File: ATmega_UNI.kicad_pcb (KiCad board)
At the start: 2 copper layers, 53.3 x 68.6 mm, 61 parts, among them J1 PDIP_1_to_14, J11 PDIP_1_to_14, J2 PDIP_15_to_28, J22 PDIP_15_to_28, J611 I2C, J612 I2C, J613 I2C, J62 4uni, J63 4uni, J64 4uni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

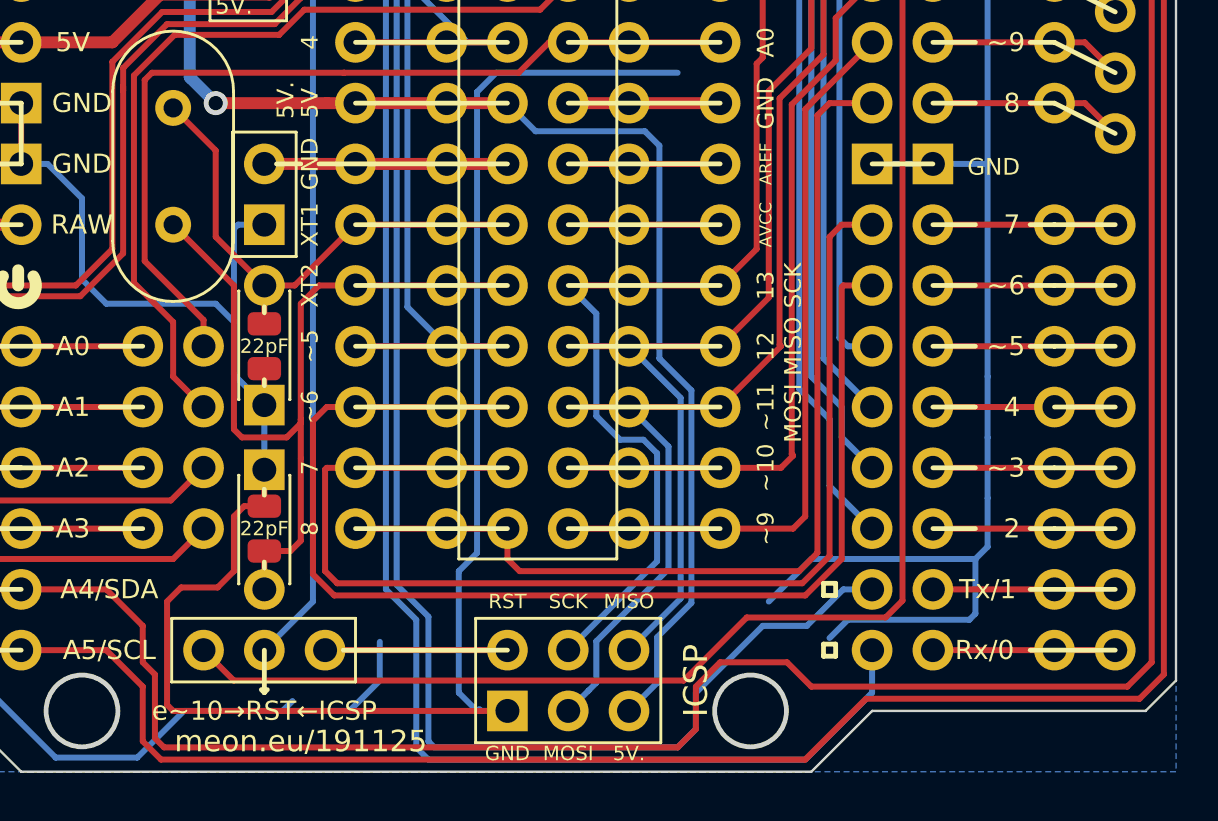
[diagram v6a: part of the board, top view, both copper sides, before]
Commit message: add one more extra gnd pin
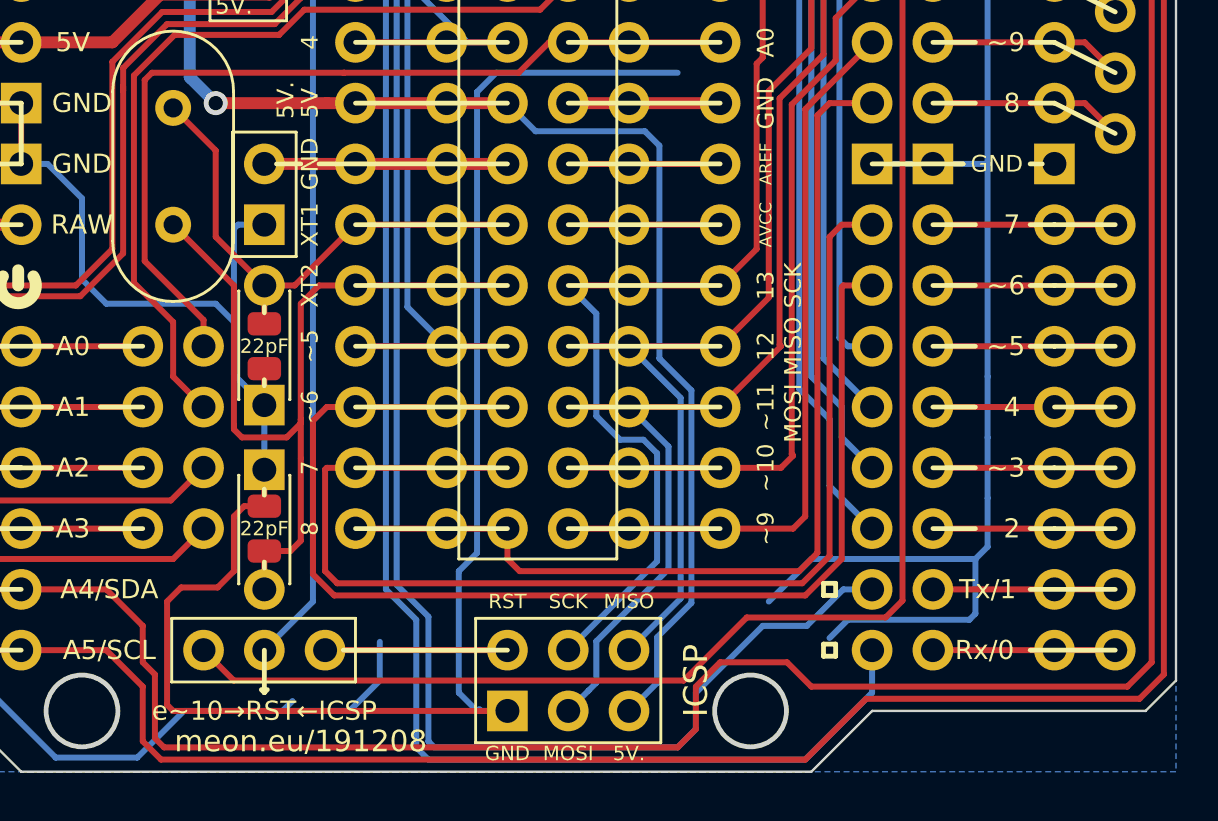
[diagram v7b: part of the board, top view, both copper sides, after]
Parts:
- added J100: extra_gnd, Connector_PinHeader_2.54mm:PinHeader_1x01_P2.54mm_Vertical_no_lines, F.Cu at (114.3, 88.9)
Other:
- board text added: "meon.eu/191208"
- board text removed: "meon.eu/191125"
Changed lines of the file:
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@@
   (general
     (thickness 1.6)
-    (drawings 580)
+    (drawings 582)
     (tracks 748)
     (zones 0)
-    (modules 61)
+    (modules 62)
     (nets 72)
   )
@@
     )
   )
+  (module Connector_PinHeader_2.54mm:PinHeader_1x01_P2.54mm_Vertical_no_lines (layer F.Cu)
+    (at 114.3 88.9)
+    (descr "Through hole straight pin header, 1x01, 2.54mm pitch, single row")
+    (tags "Through hole pin header THT 1x01 2.54mm single row")
+    (fp_text reference J100 (at 0 -2.33) (layer F.SilkS) hide
+      (effects (font (size 1 1) (thickness 0.15)))
+    )
+    (fp_text value extra_gnd (at 0 2.33) (layer F.Fab) hide
+      (effects (font (size 1 1) (thickness 0.15)))
+    )
+    (fp_line (start -0.635 -1.27) (end 1.27 -1.27) (layer F.Fab) (width 0.1))
+    (fp_line (start 1.27 -1.27) (end 1.27 1.27) (layer F.Fab) (width 0.1))
+    (fp_line (start 1.27 1.27) (end -1.27 1.27) (layer F.Fab) (width 0.1))
+    (fp_line (start -1.27 1.27) (end -1.27 -0.635) (layer F.Fab) (width 0.1))
+    (fp_line (start -1.27 -0.635) (end -0.635 -1.27) (layer F.Fab) (width 0.1))
+    (fp_line (start -1.8 -1.8) (end -1.8 1.8) (layer F.CrtYd) (width 0.05))
+    (fp_line (start -1.8 1.8) (end 1.8 1.8) (layer F.CrtYd) (width 0.05))
+    (fp_line (start 1.8 1.8) (end 1.8 -1.8) (layer F.CrtYd) (width 0.05))
+    (fp_line (start 1.8 -1.8) (end -1.8 -1.8) (layer F.CrtYd) (width 0.05))
+    (fp_text user %R (at 0 0 90) (layer F.Fab) hide
+      (effects (font (size 1 1) (thickness 0.15)))
+    )
+    (pad 1 thru_hole rect (at 0 0) (size 1.7 1.7) (drill 1) (layers *.Cu *.Mask)
+      (net 23 GND))
+    (model ${KISYS3DMOD}/Connector_PinHeader_2.54mm.3dshapes/PinHeader_1x01_P2.54mm_Vertical.wrl
+      (at (xyz 0 0 0))
+      (scale (xyz 1 1 1))
+      (rotate (xyz 0 0 0))
+    )
+  )
+  (gr_line (start 113.284 88.9) (end 113.792 88.9) (layer B.SilkS) (width 0.2))
+  (gr_line (start 113.284 88.9) (end 113.792 88.9) (layer F.SilkS) (width 0.2))
   (gr_line (start 75.692 70.612) (end 76.708 70.612) (layer B.SilkS) (width 0.2))
   (gr_line (start 75.692 70.612) (end 76.708 70.612) (layer F.SilkS) (width 0.2))
@@
   (gr_line (start 82.042 62.23) (end 85.217 62.23) (layer F.SilkS) (width 0.2))
   (gr_line (start 82.042 64.77) (end 85.217 64.77) (layer F.SilkS) (width 0.2))
-  (gr_text GND (at 111.76 89.027) (layer B.SilkS)
+  (gr_text GND (at 111.887 88.9) (layer B.SilkS)
     (effects (font (size 0.7 0.7) (thickness 0.15)) (justify mirror))
   )
-  (gr_text GND (at 111.76 89.027) (layer F.SilkS)
+  (gr_text GND (at 111.887 88.9) (layer F.SilkS)
     (effects (font (size 0.7 0.7) (thickness 0.15)))
   )
@@
     (effects (font (size 0.7 0.7) (thickness 0.15)))
   )
-  (gr_line (start 106.68 88.9) (end 109.22 88.9) (layer B.SilkS) (width 0.2))
-  (gr_line (start 106.68 88.9) (end 109.22 88.9) (layer F.SilkS) (width 0.2))
-  (gr_text meon.eu/191125 (at 82.804 113.03) (layer F.SilkS)
+  (gr_line (start 106.68 88.9) (end 110.49 88.9) (layer B.SilkS) (width 0.2))
+  (gr_line (start 106.68 88.9) (end 110.49 88.9) (layer F.SilkS) (width 0.2))
+  (gr_text meon.eu/191208 (at 82.804 113.03) (layer F.SilkS)
     (effects (font (size 0.9 0.9) (thickness 0.2)))
   )
@@
     (effects (font (size 0.7 0.7) (thickness 0.15)))
   )
-  (gr_text meon.eu/191125 (at 82.804 113.03) (layer B.SilkS)
+  (gr_text meon.eu/191208 (at 82.804 113.03) (layer B.SilkS)
     (effects (font (size 0.9 0.9) (thickness 0.2)) (justify mirror))
   )

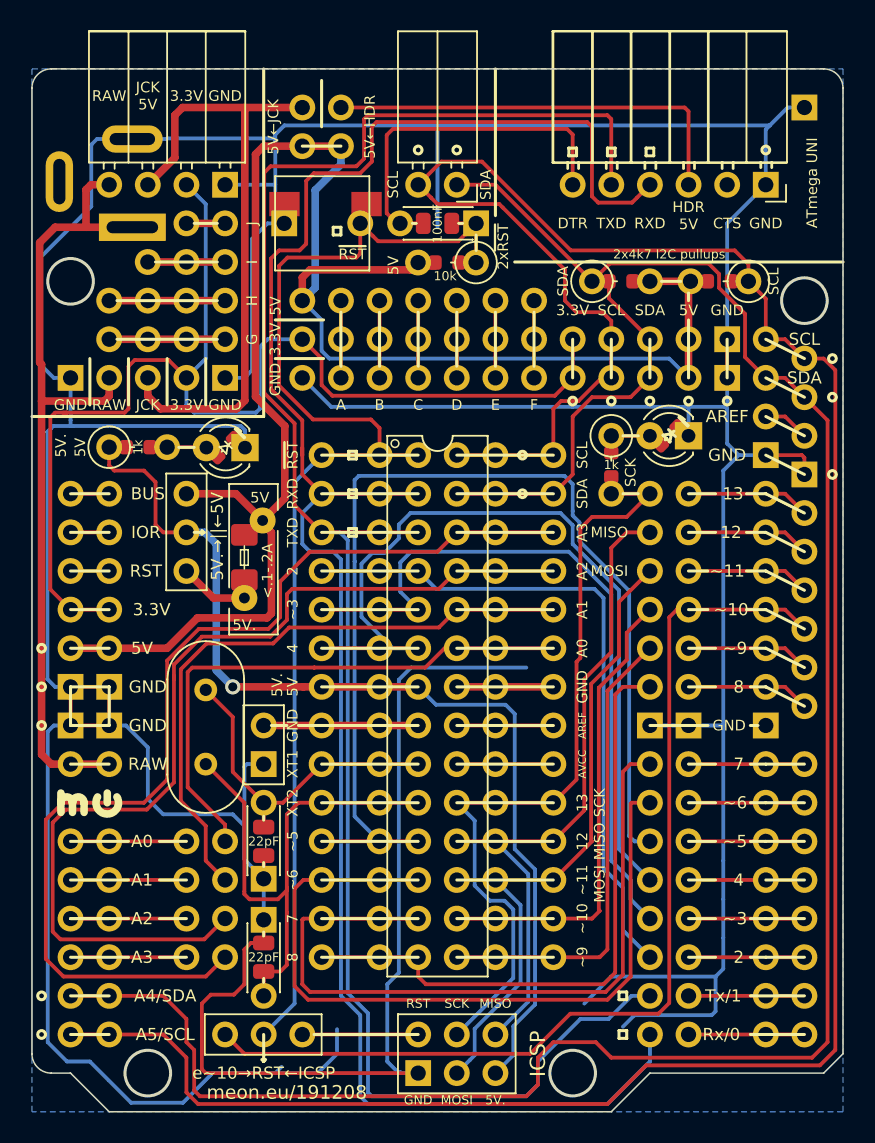
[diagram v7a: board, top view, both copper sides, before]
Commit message: move smt switch away from 5V pins
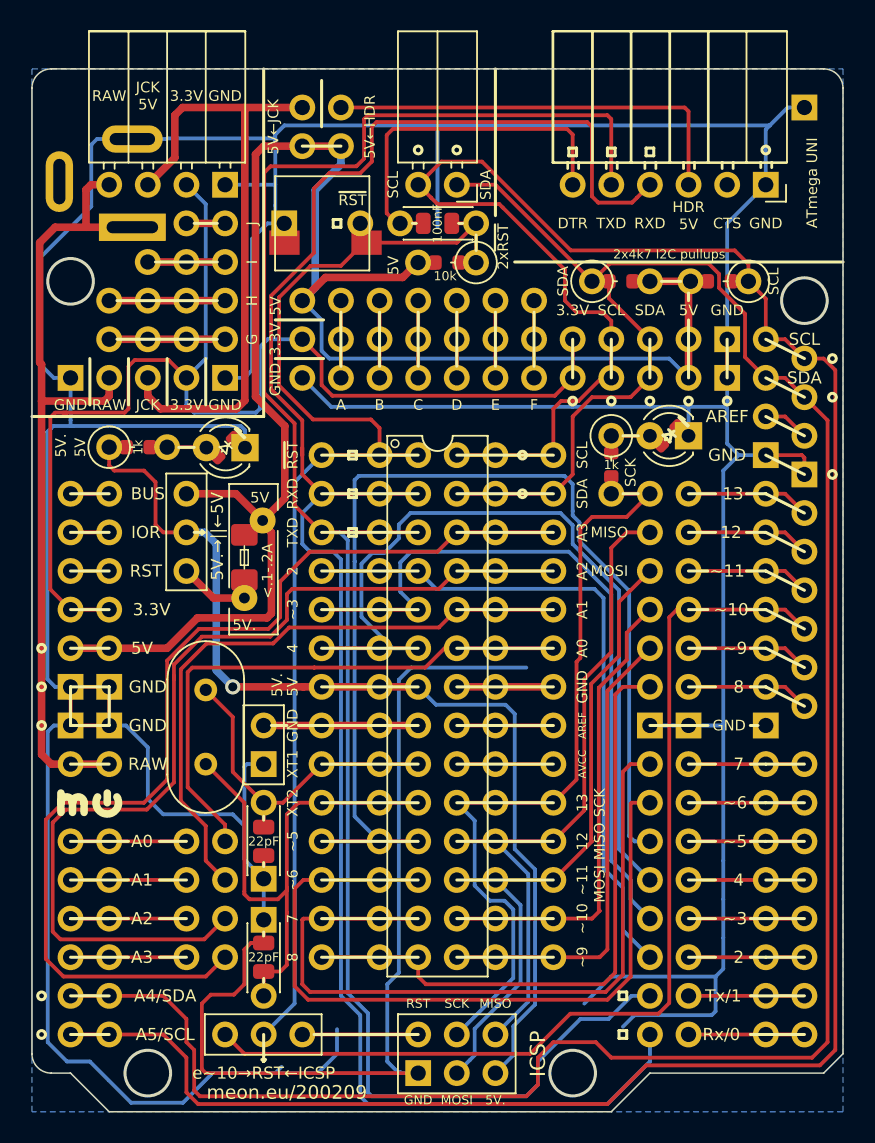
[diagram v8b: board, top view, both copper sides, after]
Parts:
- moved SW2 2.54 mm to (85.3, 57.1)
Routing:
- net ~RST: track 86.9 -> 83.1 mm
- net RXD: track 126.2 -> 124.9 mm
- net GND: track 400.2 -> 399.1 mm
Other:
- board text added: "meon.eu/200209"
- board text removed: "meon.eu/191208"
